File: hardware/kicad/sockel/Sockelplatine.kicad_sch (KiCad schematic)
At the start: 12 parts, among them J1 24V Eingang, J2 Stapelstecker 2x20, J3 Kettenstecker, Stift SMD (tre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, J4 Leistungsstecker, Stift SMD (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, U1 Raspberry Pi Pico, U2 K7805-2000R3

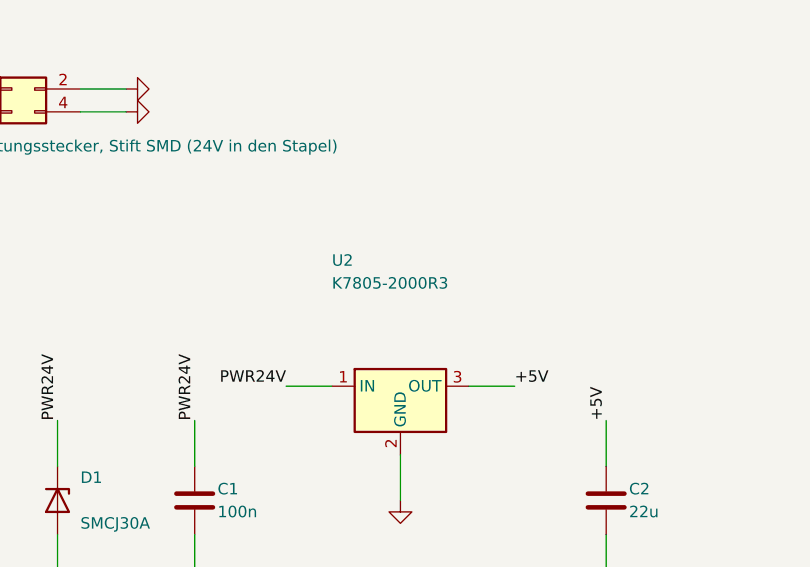
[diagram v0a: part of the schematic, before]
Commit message: Sockel: U2 auf K7805-1000R3 (C909765) -- der 2-A-Namensvetter war eine Falle
Runde 3 der U2-Odyssee: C2931187 (DEXU 2A) abgekuendigt; der gestern
eingetragene Ersatz C5378008 (JETEKPS 'K7805-2000R3') vertraegt laut
LCSC-Rohdaten nur 7-18 V Eingang -- gleiche Typenbezeichnung, an 24 V
unbrauchbar. Bestueckt wird der 1-A-Bruder der DEXU-Baureihe:
Datenblatt K78xx-1000R3 (REV A0-2018.12) selbst gelesen, K7805-1000R3
Eingang 6.0-30 V (24 nominal). 1 A traegt die reine Logik-Schiene
(Lastbudget im Kommentar, Worst Case ~0,5 A). Der Quelltext-Grep-Test
('Sockel ist kein Modul') blieb dabei absichtlich unangetastet.

Co-Authored-By: Claude Fable 5 <noreply@anthropic.com>
Claude-Session: https://claude.ai/code/session_01KDus95JJwCeRuwccgBWEi5
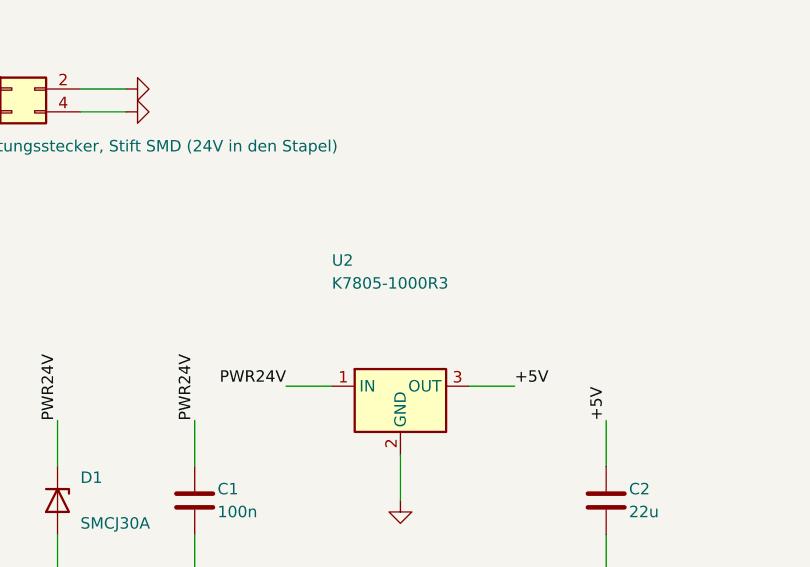
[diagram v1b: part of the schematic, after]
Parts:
- U2: value K7805-2000R3 -> K7805-1000R3
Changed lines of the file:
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@@
 		(instances
 			(project "Sockelplatine"
-				(path "/c8027639-4277-4c00-9583-c715fce0061c"
+				(path "/d02c803c-228f-40f0-84e5-866de0ef4b74"
 					(reference "J1")
 					(unit 1)
@@
 		(instances
 			(project "Sockelplatine"
-				(path "/c8027639-4277-4c00-9583-c715fce0061c"
+				(path "/d02c803c-228f-40f0-84e5-866de0ef4b74"
 					(reference "#FLG1")
 					(unit 1)
@@
 		(instances
 			(project "Sockelplatine"
-				(path "/c8027639-4277-4c00-9583-c715fce0061c"
+				(path "/d02c803c-228f-40f0-84e5-866de0ef4b74"
 					(reference "D1")
 					(unit 1)
@@
 		(instances
 			(project "Sockelplatine"
-				(path "/c8027639-4277-4c00-9583-c715fce0061c"
+				(path "/d02c803c-228f-40f0-84e5-866de0ef4b74"
 					(reference "C3")
 					(unit 1)
@@
 		(instances
 			(project "Sockelplatine"
-				(path "/c8027639-4277-4c00-9583-c715fce0061c"
+				(path "/d02c803c-228f-40f0-84e5-866de0ef4b74"
 					(reference "C1")
 					(unit 1)
@@
 			)
 		)
-		(property "Value" "K7805-2000R3"
+		(property "Value" "K7805-1000R3"
 			(at 116.84 99.06 0)
 			(show_name no)
@@
 		(instances
 			(project "Sockelplatine"
-				(path "/c8027639-4277-4c00-9583-c715fce0061c"
+				(path "/d02c803c-228f-40f0-84e5-866de0ef4b74"
 					(reference "U2")
 					(unit 1)
@@
 		(instances
 			(project "Sockelplatine"
-				(path "/c8027639-4277-4c00-9583-c715fce0061c"
+				(path "/d02c803c-228f-40f0-84e5-866de0ef4b74"
 					(reference "C2")
 					(unit 1)
@@
 		(instances
 			(project "Sockelplatine"
-				(path "/c8027639-4277-4c00-9583-c715fce0061c"
+				(path "/d02c803c-228f-40f0-84e5-866de0ef4b74"
 					(reference "J4")
 					(unit 1)
@@
 		(instances
 			(project "Sockelplatine"
-				(path "/c8027639-4277-4c00-9583-c715fce0061c"
+				(path "/d02c803c-228f-40f0-84e5-866de0ef4b74"
 					(reference "J3")
 					(unit 1)
@@
 		(instances
 			(project "Sockelplatine"
-				(path "/c8027639-4277-4c00-9583-c715fce0061c"
+				(path "/d02c803c-228f-40f0-84e5-866de0ef4b74"
 					(reference "J2")
 					(unit 1)
@@
 		(instances
 			(project "Sockelplatine"
-				(path "/c8027639-4277-4c00-9583-c715fce0061c"
+				(path "/d02c803c-228f-40f0-84e5-866de0ef4b74"
 					(reference "U1")
 					(unit 1)
@@
 		(instances
 			(project "Sockelplatine"
-				(path "/c8027639-4277-4c00-9583-c715fce0061c"
+				(path "/d02c803c-228f-40f0-84e5-866de0ef4b74"
 					(reference "R1")
 					(unit 1)
@@
 		(instances
 			(project "Sockelplatine"
-				(path "/c8027639-4277-4c00-9583-c715fce0061c"
+				(path "/d02c803c-228f-40f0-84e5-866de0ef4b74"
 					(reference "R2")
 					(unit 1)
@@
 		(instances
 			(project "Sockelplatine"
-				(path "/c8027639-4277-4c00-9583-c715fce0061c"
+				(path "/d02c803c-228f-40f0-84e5-866de0ef4b74"
 					(reference "#PWR177")
 					(unit 1)
@@
 		(instances
 			(project "Sockelplatine"
-				(path "/c8027639-4277-4c00-9583-c715fce0061c"
+				(path "/d02c803c-228f-40f0-84e5-866de0ef4b74"
 					(reference "#PWR179")
 					(unit 1)
@@
 		(instances
 			(project "Sockelplatine"
-				(path "/c8027639-4277-4c00-9583-c715fce0061c"
+				(path "/d02c803c-228f-40f0-84e5-866de0ef4b74"
 					(reference "#PWR181")
 					(unit 1)
@@
 		(instances
 			(project "Sockelplatine"
-				(path "/c8027639-4277-4c00-9583-c715fce0061c"
+				(path "/d02c803c-228f-40f0-84e5-866de0ef4b74"
 					(reference "#PWR183")
 					(unit 1)
@@
 		(instances
 			(project "Sockelplatine"
-				(path "/c8027639-4277-4c00-9583-c715fce0061c"
+				(path "/d02c803c-228f-40f0-84e5-866de0ef4b74"
 					(reference "#PWR185")
 					(unit 1)
@@
 		(instances
 			(project "Sockelplatine"
-				(path "/c8027639-4277-4c00-9583-c715fce0061c"
+				(path "/d02c803c-228f-40f0-84e5-866de0ef4b74"
 					(reference "#PWR187")
 					(unit 1)
@@
 		(instances
 			(project "Sockelplatine"
-				(path "/c8027639-4277-4c00-9583-c715fce0061c"
+				(path "/d02c803c-228f-40f0-84e5-866de0ef4b74"
 					(reference "#PWR189")
 					(unit 1)
@@
 		(instances
 			(project "Sockelplatine"
-				(path "/c8027639-4277-4c00-9583-c715fce0061c"
+				(path "/d02c803c-228f-40f0-84e5-866de0ef4b74"
 					(reference "#PWR191")
 					(unit 1)
@@
 		(instances
 			(project "Sockelplatine"
-				(path "/c8027639-4277-4c00-9583-c715fce0061c"
+				(path "/d02c803c-228f-40f0-84e5-866de0ef4b74"
 					(reference "#PWR193")
 					(unit 1)
@@
 		(instances
 			(project "Sockelplatine"
-				(path "/c8027639-4277-4c00-9583-c715fce0061c"
+				(path "/d02c803c-228f-40f0-84e5-866de0ef4b74"
 					(reference "#PWR195")
 					(unit 1)
@@
 		(instances
 			(project "Sockelplatine"
-				(path "/c8027639-4277-4c00-9583-c715fce0061c"
+				(path "/d02c803c-228f-40f0-84e5-866de0ef4b74"
 					(reference "#PWR197")
 					(unit 1)
@@
 		(instances
 			(project "Sockelplatine"
-				(path "/c8027639-4277-4c00-9583-c715fce0061c"
+				(path "/d02c803c-228f-40f0-84e5-866de0ef4b74"
 					(reference "#PWR199")
 					(unit 1)
@@
 		(instances
 			(project "Sockelplatine"
-				(path "/c8027639-4277-4c00-9583-c715fce0061c"
+				(path "/d02c803c-228f-40f0-84e5-866de0ef4b74"
 					(reference "#PWR201")
 					(unit 1)
@@
 		(instances
 			(project "Sockelplatine"
-				(path "/c8027639-4277-4c00-9583-c715fce0061c"
+				(path "/d02c803c-228f-40f0-84e5-866de0ef4b74"
 					(reference "#PWR203")
 					(unit 1)
@@
 		(instances
 			(project "Sockelplatine"
-				(path "/c8027639-4277-4c00-9583-c715fce0061c"
+				(path "/d02c803c-228f-40f0-84e5-866de0ef4b74"
 					(reference "#PWR205")
 					(unit 1)
@@
 		(instances
 			(project "Sockelplatine"
-				(path "/c8027639-4277-4c00-9583-c715fce0061c"
+				(path "/d02c803c-228f-40f0-84e5-866de0ef4b74"
 					(reference "#PWR207")
 					(unit 1)
@@
 		(instances
 			(project "Sockelplatine"
-				(path "/c8027639-4277-4c00-9583-c715fce0061c"
+				(path "/d02c803c-228f-40f0-84e5-866de0ef4b74"
 					(reference "#PWR209")
 					(unit 1)
@@
 		(instances
 			(project "Sockelplatine"
-				(path "/c8027639-4277-4c00-9583-c715fce0061c"
+				(path "/d02c803c-228f-40f0-84e5-866de0ef4b74"
 					(reference "#PWR211")
 					(unit 1)
@@
 		(instances
 			(project "Sockelplatine"
-				(path "/c8027639-4277-4c00-9583-c715fce0061c"
+				(path "/d02c803c-228f-40f0-84e5-866de0ef4b74"
 					(reference "#PWR213")
 					(unit 1)
@@
 		(instances
 			(project "Sockelplatine"
-				(path "/c8027639-4277-4c00-9583-c715fce0061c"
+				(path "/d02c803c-228f-40f0-84e5-866de0ef4b74"
 					(reference "#PWR215")
 					(unit 1)
@@
 		(instances
 			(project "Sockelplatine"
-				(path "/c8027639-4277-4c00-9583-c715fce0061c"
+				(path "/d02c803c-228f-40f0-84e5-866de0ef4b74"
 					(reference "#PWR217")
 					(unit 1)
@@
 		(instances
 			(project "Sockelplatine"
-				(path "/c8027639-4277-4c00-9583-c715fce0061c"
+				(path "/d02c803c-228f-40f0-84e5-866de0ef4b74"
 					(reference "#PWR219")
 					(unit 1)
